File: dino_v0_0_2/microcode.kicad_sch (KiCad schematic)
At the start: 4 parts, among them U15 AT28C64B, U16 74LS244N, U17 74LS244N, U9 AT28C64B

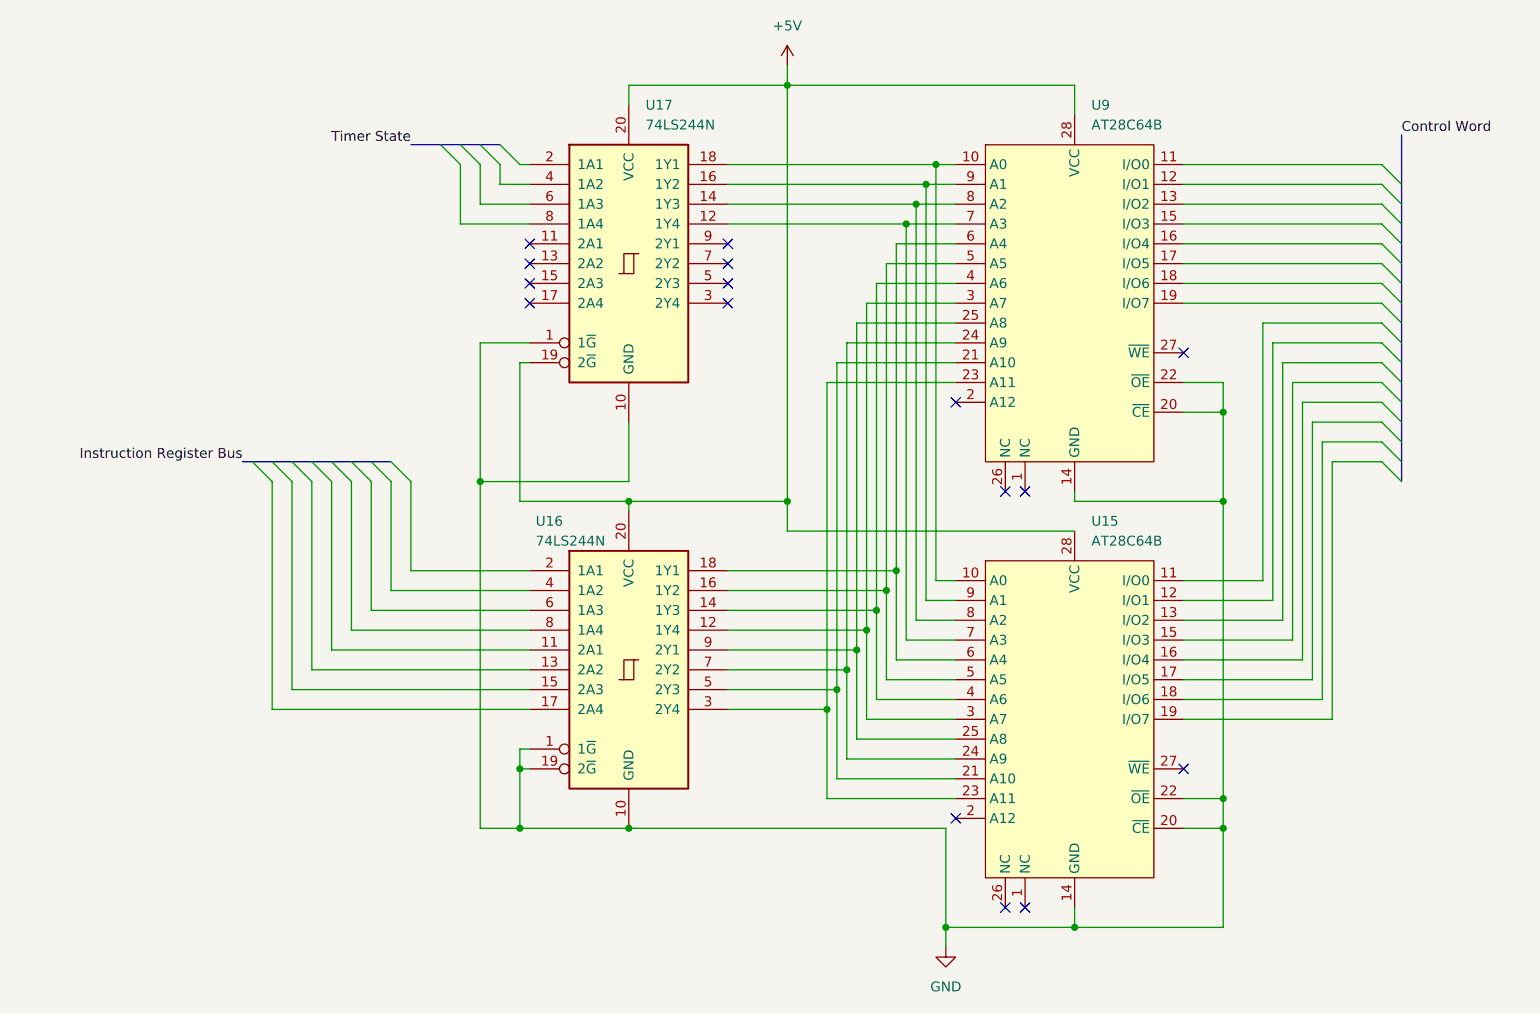
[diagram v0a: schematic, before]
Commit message: DINO v0.0.3: complete ALU/control-word, add MAR+reset sheets, wire reset circuit
ALU sheet: flags register moved from '173 (not in stock) to '273 + a '157
mux to emulate the missing load-enable pins; Z-detect built from a NOR+AND
De Morgan tree instead of a '260; ALU_CIN built from NAND(SA1,SA0) reusing
two already-placed spare gates instead of a dedicated XOR/'86. Sheet is
now fully wired and netlist-clean.

Control word sheet: all 16 CW bits assigned and wired (3x '138 decoders
for the load/source/misc fields, direct bus taps for HALT/PC_MAR_MUX/
PC_UP/END and the ALU SA[2:0] select). Found and fixed several cross-
sheet signal-name mismatches this uncovered (OUT_REG_LOAD/REG_OUT_LOAD,
PC_MAR_MUX/PC_MUX, T-state counter labels, a mirror-reversed IRB->ROM-
address buffer in microcode).

New: MAR and reset sheets, wired into the root hierarchy. Reset circuit
is a from-scratch design: RC+button+74HC14 Schmitt front end feeds the
async PRESET of the clock cluster's spare '74 half (U27B), synchronizing
release to CLK; its Q/~Q fan out to the flags register, the T-state
counter's clear, and (OR'd with the existing microcode-driven PC_CLEAR,
reusing spare gates on the same '02) the PC counters' clear.

Deprecated 7 schematic files no longer referenced by the root sheet's
hierarchy into dino_v0_0_2/deprecated/. Added docs/notes/kicad_netlist.py,
a .kicad_sch connectivity auditor (pin/net resolution incl. buses and
same-name local-label merging) used throughout this session to find the
above bugs; archived completed-work docs into docs/notes/Done/ and
rewrote dino_session_state.md as the current authoritative state+TODO.

Co-Authored-By: Claude Sonnet 5 <noreply@anthropic.com>
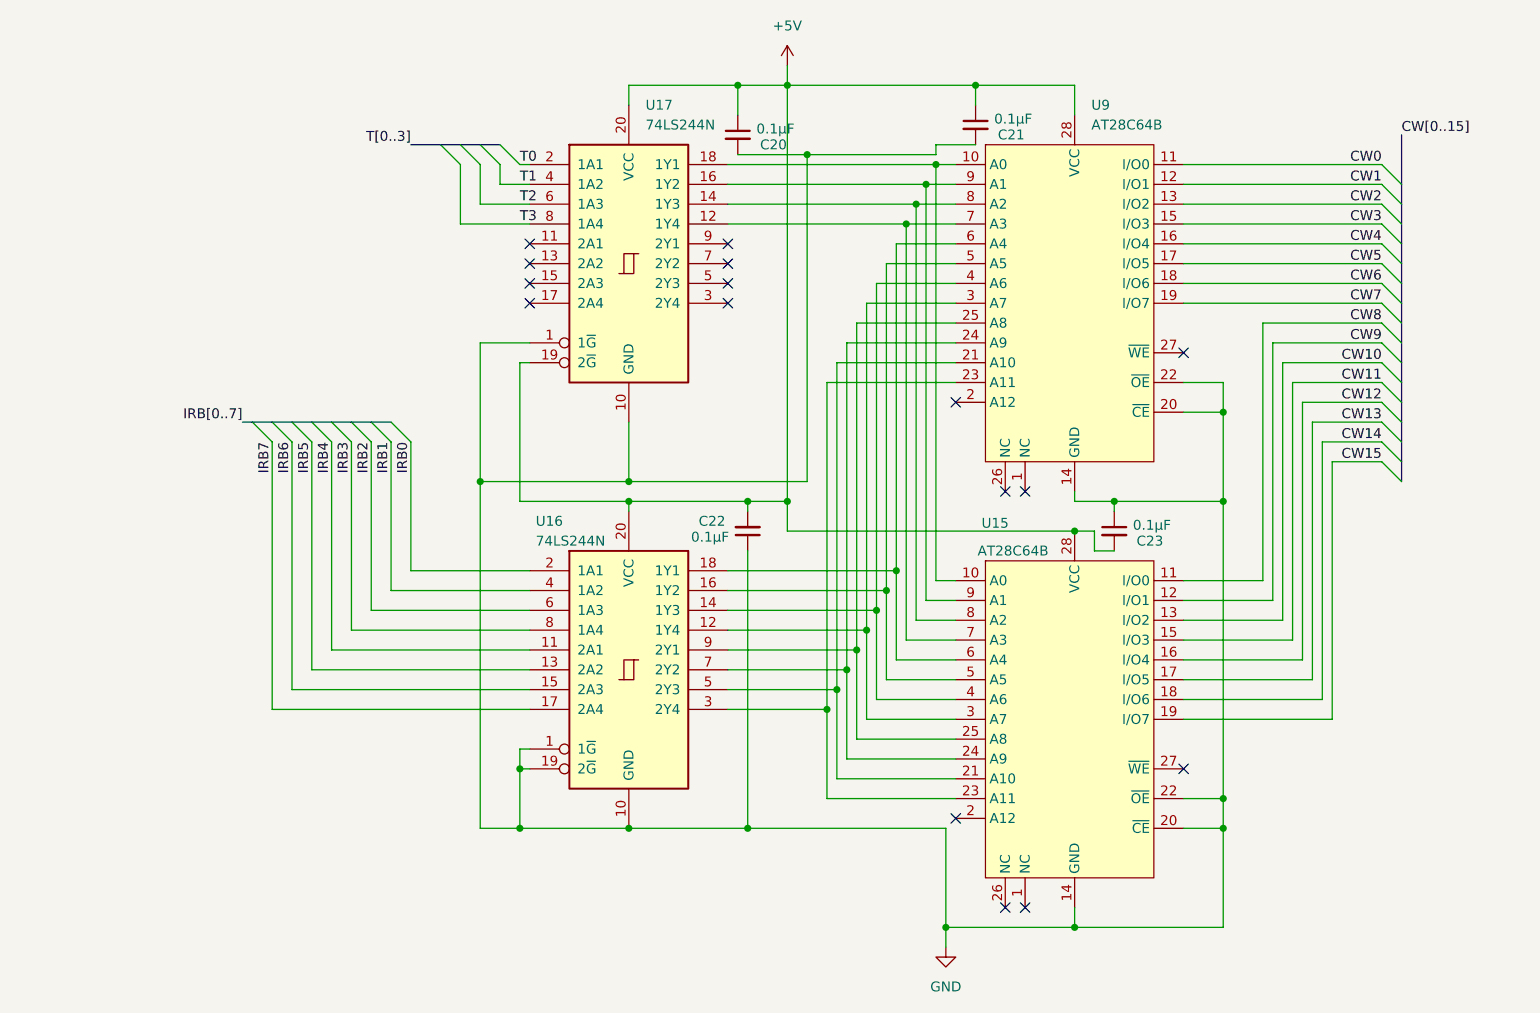
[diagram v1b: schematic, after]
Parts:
- added C20, C21, C22, C23: 0.1µF, symbol Device:C_Small
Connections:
- net +5V: now also C20.1, C21.1, C22.2, C23.2
- net GND: now also C20.2, C21.2, C22.1, C23.1
- net CW8: now reaches U15.11 (I/O0)
- net CW9: now reaches U15.12 (I/O1)
- net CW10: now reaches U15.13 (I/O2)
- net CW11: now reaches U15.15 (I/O3)
- net CW12: now reaches U15.16 (I/O4)
- net CW13: now reaches U15.17 (I/O5)
- net CW14: now reaches U15.18 (I/O6)
- net CW15: now reaches U15.19 (I/O7)
- net CW0: now reaches U9.11 (I/O0)
- net CW1: now reaches U9.12 (I/O1)
- net CW2: now reaches U9.13 (I/O2)
- net CW3: now reaches U9.15 (I/O3)
- net CW4: now reaches U9.16 (I/O4)
- net CW5: now reaches U9.17 (I/O5)
- net CW6: now reaches U9.18 (I/O6)
- net CW7: now reaches U9.19 (I/O7)
- net T0: now reaches U17.2 (1A1)
- net T1: now reaches U17.4 (1A2)
- net T2: now reaches U17.6 (1A3)
- net T3: now reaches U17.8 (1A4)
- net IRB4: now reaches U16.11 (2A1)
- net IRB5: now reaches U16.13 (2A2)
- net IRB6: now reaches U16.15 (2A3)
- net IRB7: now reaches U16.17 (2A4)
- net IRB0: now reaches U16.2 (1A1)
- net IRB1: now reaches U16.4 (1A2)
- net IRB2: now reaches U16.6 (1A3)
- net IRB3: now reaches U16.8 (1A4)
